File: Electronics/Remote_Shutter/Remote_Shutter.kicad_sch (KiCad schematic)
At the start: 15 parts, among them J1 OLED, J2 Joystick, J3 Micro Lipo pins, J4 AudioJack3, SW1 SW_SPDT, SW2 SW_SPDT, U1 Xiao, U2 PC817, U3 PC817

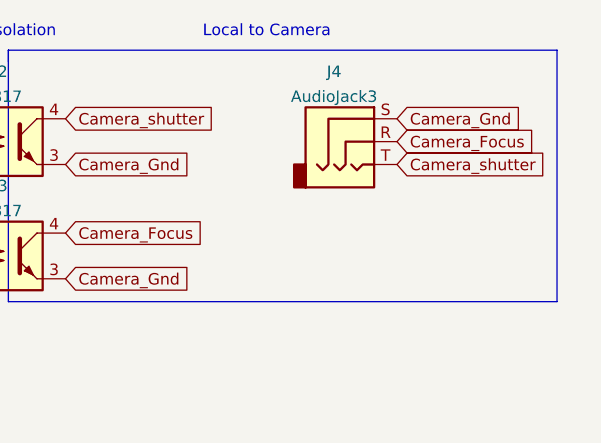
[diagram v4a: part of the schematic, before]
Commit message: fixed footprint for the TRS also made the PCB smaller and routed it.
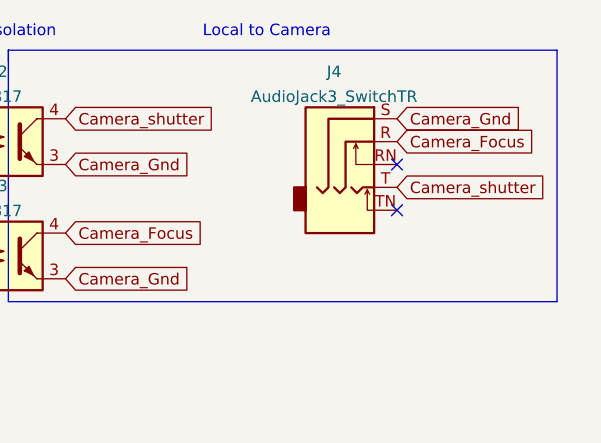
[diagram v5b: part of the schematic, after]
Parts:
- removed J4: AudioJack3, cubepattern:CUI_SJ1-3514, symbol Connector:AudioJack3
- added J4: AudioJack3_SwitchTR, cubepattern:SWITCHCRAFT_35RAPC2BH3, symbol Connector:AudioJack3_SwitchTR
- R1, R2, R3, R4: footprint Resistor_THT:R_Axial_DIN0207_L6.3mm_D2.5mm_P10.16mm_Horizontal -> Resistor_THT:R_Axial_DIN0204_L3.6mm_D1.6mm_P7.62mm_Horizontal
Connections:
- net Camera_Focus: now also J4.R
- net Camera_Gnd: now also J4.S
- net Camera_shutter: now also J4.T
- no-connect marks 4 -> 6
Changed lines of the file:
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@@
   (no_connect (at 40.64 19.05))
   (no_connect (at 43.18 19.05))
+  (no_connect (at 148.59 35.56))
+  (no_connect (at 148.59 30.48))
   (wire (pts (xy 91.44 38.1) (xy 96.52 38.1))
     (stroke (width 0) (type default) (color 0 0 0 0))
@@
     (stroke (width 0) (type default) (color 0 0 0 0))
   )
+  (wire (pts (xy 78.74 63.5) (xy 78.74 68.58))
+    (stroke (width 0) (type default) (color 0 0 0 0))
+  )
+  (wire (pts (xy 74.93 59.69) (xy 78.74 59.69))
+    (stroke (width 0) (type default) (color 0 0 0 0))
+  )
+  (polyline (pts (xy 166.37 17.78) (xy 105.41 17.78))
+    (stroke (width 0) (type default) (color 0 0 0 0))
+  )
+  (wire (pts (xy 86.36 30.48) (xy 96.52 30.48))
+    (stroke (width 0) (type default) (color 0 0 0 0))
+  )
+  (polyline (pts (xy 105.41 17.78) (xy 105.41 19.05))
+    (stroke (width 0) (type default) (color 0 0 0 0))
+  )
+  (wire (pts (xy 59.69 52.07) (xy 49.53 52.07))
+    (stroke (width 0) (type default) (color 0 0 0 0))
+  )
+  (polyline (pts (xy 15.24 71.12) (xy 15.24 60.96))
+    (stroke (width 0) (type default) (color 0 0 0 0))
+  )
   (wire (pts (xy 78.74 59.69) (xy 78.74 63.5))
-    (stroke (width 0) (type default) (color 0 0 0 0))
-  )
-  (wire (pts (xy 74.93 59.69) (xy 78.74 59.69))
-    (stroke (width 0) (type default) (color 0 0 0 0))
-  )
-  (polyline (pts (xy 166.37 17.78) (xy 105.41 17.78))
-    (stroke (width 0) (type default) (color 0 0 0 0))
-  )
-  (wire (pts (xy 86.36 30.48) (xy 96.52 30.48))
-    (stroke (width 0) (type default) (color 0 0 0 0))
-  )
-  (polyline (pts (xy 105.41 17.78) (xy 105.41 19.05))
-    (stroke (width 0) (type default) (color 0 0 0 0))
-  )
-  (wire (pts (xy 59.69 52.07) (xy 49.53 52.07))
-    (stroke (width 0) (type default) (color 0 0 0 0))
-  )
-  (polyline (pts (xy 15.24 71.12) (xy 15.24 60.96))
-    (stroke (width 0) (type default) (color 0 0 0 0))
-  )
-  (wire (pts (xy 78.74 63.5) (xy 78.74 68.58))
     (stroke (width 0) (type default) (color 0 0 0 0))
   )
@@
     )
   )
-  (global_label "Camera_shutter" (shape input) (at 148.59 30.48 0) (fields_autoplaced)
-    (effects (font (size 1.27 1.27)) (justify left))
-    (property "Intersheet References" "${INTERSHEET_REFS}" (id 0) (at 165.7593 30.4006 0)
+  (global_label "Camera_shutter" (shape input) (at 148.59 33.02 0) (fields_autoplaced)
+    (effects (font (size 1.27 1.27)) (justify left))
+    (property "Intersheet References" "${INTERSHEET_REFS}" (id 0) (at 165.7593 32.9406 0)
       (effects (font (size 1.27 1.27)) (justify left) hide)
     )
@@
   (symbol (lib_id "power:+5V") (at 24.13 49.53 90) (unit 1)
     (in_bom yes) (on_board yes) (fields_autoplaced)
-    (property "Reference" "#PWR?" (id 0) (at 27.94 49.53 0)
+    (property "Reference" "#PWR0102" (id 0) (at 27.94 49.53 0)
       (effects (font (size 1.27 1.27)) hide)
     )
@@
     )
     (pin "1")
+  )
+  (symbol (lib_id "Connector:AudioJack3_SwitchTR") (at 143.51 27.94 0) (unit 1)
+    (in_bom yes) (on_board yes) (fields_autoplaced)
+    (property "Reference" "J4" (id 0) (at 141.605 20.1635 0))
+    (property "Value" "AudioJack3_SwitchTR" (id 1) (at 141.605 22.9386 0))
+    (property "Footprint" "cubepattern:SWITCHCRAFT_35RAPC2BH3" (id 2) (at 143.51 27.94 0)
+      (effects (font (size 1.27 1.27)) hide)
+    )
+    (property "Datasheet" "~" (id 3) (at 143.51 27.94 0)
+      (effects (font (size 1.27 1.27)) hide)
+    )
+    (pin "R")
+    (pin "RN")
+    (pin "S")
+    (pin "T")
+    (pin "TN")
   )
   (symbol (lib_id "Device:R_Small") (at 88.9 38.1 90) (unit 1)
@@
     (property "Reference" "R4" (id 0) (at 88.9 33.3969 90))
     (property "Value" "220ohm" (id 1) (at 88.9 36.172 90))
-    (property "Footprint" "Resistor_THT:R_Axial_DIN0207_L6.3mm_D2.5mm_P10.16mm_Horizontal" (id 2) (at 88.9 38.1 0)
+    (property "Footprint" "Resistor_THT:R_Axial_DIN0204_L3.6mm_D1.6mm_P7.62mm_Horizontal" (id 2) (at 88.9 38.1 0)
       (effects (font (size 1.27 1.27)) hide)
     )
@@
     (property "Reference" "R3" (id 0) (at 88.9 20.6969 90))
     (property "Value" "220ohm" (id 1) (at 88.9 23.472 90))
-    (property "Footprint" "Resistor_THT:R_Axial_DIN0207_L6.3mm_D2.5mm_P10.16mm_Horizontal" (id 2) (at 88.9 25.4 0)
+    (property "Footprint" "Resistor_THT:R_Axial_DIN0204_L3.6mm_D1.6mm_P7.62mm_Horizontal" (id 2) (at 88.9 25.4 0)
       (effects (font (size 1.27 1.27)) hide)
     )
@@
   (symbol (lib_id "power:GND") (at 24.13 52.07 270) (unit 1)
     (in_bom yes) (on_board yes) (fields_autoplaced)
-    (property "Reference" "#PWR?" (id 0) (at 17.78 52.07 0)
+    (property "Reference" "#PWR0101" (id 0) (at 17.78 52.07 0)
       (effects (font (size 1.27 1.27)) hide)
     )
@@
     (property "Reference" "R1" (id 0) (at 62.23 54.9869 90))
     (property "Value" "75ohm" (id 1) (at 62.23 57.762 90))
-    (property "Footprint" "Resistor_THT:R_Axial_DIN0207_L6.3mm_D2.5mm_P10.16mm_Horizontal" (id 2) (at 62.23 59.69 0)
+    (property "Footprint" "Resistor_THT:R_Axial_DIN0204_L3.6mm_D1.6mm_P7.62mm_Horizontal" (id 2) (at 62.23 59.69 0)
       (effects (font (size 1.27 1.27)) hide)
     )
@@
     (pin "1")
     (pin "2")
-  )
-  (symbol (lib_id "Connector:AudioJack3") (at 143.51 27.94 0) (unit 1)
-    (in_bom yes) (on_board yes) (fields_autoplaced)
-    (property "Reference" "J4" (id 0) (at 141.605 20.1635 0))
-    (property "Value" "AudioJack3" (id 1) (at 141.605 22.9386 0))
-    (property "Footprint" "cubepattern:CUI_SJ1-3514" (id 2) (at 143.51 27.94 0)
-      (effects (font (size 1.27 1.27)) hide)
-    )
-    (property "Datasheet" "~" (id 3) (at 143.51 27.94 0)
-      (effects (font (size 1.27 1.27)) hide)
-    )
-    (pin "R")
-    (pin "S")
-    (pin "T")
   )
   (symbol (lib_id "power:GND") (at 88.9 60.96 90) (unit 1)
@@
     (property "Reference" "R2" (id 0) (at 62.23 63.8769 90))
     (property "Value" "10ohm" (id 1) (at 62.23 66.652 90))
-    (property "Footprint" "Resistor_THT:R_Axial_DIN0207_L6.3mm_D2.5mm_P10.16mm_Horizontal" (id 2) (at 62.23 68.58 0)
+    (property "Footprint" "Resistor_THT:R_Axial_DIN0204_L3.6mm_D1.6mm_P7.62mm_Horizontal" (id 2) (at 62.23 68.58 0)
       (effects (font (size 1.27 1.27)) hide)
     )
@@
   )
   (symbol_instances
+    (path "/b4f4fd8c-2bd4-42bb-83f4-91cfb4502a52"
+      (reference "#PWR0101") (unit 1) (value "GND") (footprint "")
+    )
+    (path "/228ec2f0-c566-4d23-b3f1-fe5d842defc4"
+      (reference "#PWR0102") (unit 1) (value "+5V") (footprint "")
+    )
     (path "/0dda9a3a-67e1-426d-8cd7-37bed7b3a5c2"
       (reference "#PWR0103") (unit 1) (value "GND") (footprint "")
@@
       (reference "#PWR0112") (unit 1) (value "GND") (footprint "")
     )
-    (path "/228ec2f0-c566-4d23-b3f1-fe5d842defc4"
-      (reference "#PWR?") (unit 1) (value "+5V") (footprint "")
-    )
-    (path "/b4f4fd8c-2bd4-42bb-83f4-91cfb4502a52"
-      (reference "#PWR?") (unit 1) (value "GND") (footprint "")
-    )
     (path "/8cb55fe4-e0f1-400c-8abb-b081e431a032"
       (reference "D1") (unit 1) (value "Red") (footprint "LED_THT:LED_D3.0mm")
@@
       (reference "J3") (unit 1) (value "Micro Lipo pins") (footprint "Connector_PinSocket_2.54mm:PinSocket_1x02_P2.54mm_Vertical")
     )
-    (path "/ca4ade4b-071e-4766-bfd1-eee3b7fe162d"
-      (reference "J4") (unit 1) (value "AudioJack3") (footprint "cubepattern:CUI_SJ1-3514")
+    (path "/25e0d0b9-b4b7-4a65-bce9-b64955e223bc"
+      (reference "J4") (unit 1) (value "AudioJack3_SwitchTR") (footprint "cubepattern:SWITCHCRAFT_35RAPC2BH3")
     )
     (path "/b8dab869-c827-4181-80d6-62cae32b4e4d"
-      (reference "R1") (unit 1) (value "75ohm") (footprint "Resistor_THT:R_Axial_DIN0207_L6.3mm_D2.5mm_P10.16mm_Horizontal")
+      (reference "R1") (unit 1) (value "75ohm") (footprint "Resistor_THT:R_Axial_DIN0204_L3.6mm_D1.6mm_P7.62mm_Horizontal")
     )
     (path "/f999f196-9de3-4cc5-a73e-ea12c61d5580"
-      (reference "R2") (unit 1) (value "10ohm") (footprint "Resistor_THT:R_Axial_DIN0207_L6.3mm_D2.5mm_P10.16mm_Horizontal")
+      (reference "R2") (unit 1) (value "10ohm") (footprint "Resistor_THT:R_Axial_DIN0204_L3.6mm_D1.6mm_P7.62mm_Horizontal")
     )
     (path "/4a583b03-7ba0-42d6-ac20-d9bd4ec5453d"
-      (reference "R3") (unit 1) (value "220ohm") (footprint "Resistor_THT:R_Axial_DIN0207_L6.3mm_D2.5mm_P10.16mm_Horizontal")
+      (reference "R3") (unit 1) (value "220ohm") (footprint "Resistor_THT:R_Axial_DIN0204_L3.6mm_D1.6mm_P7.62mm_Horizontal")
     )
     (path "/2a88d07d-3256-48f8-9a69-efbd4975a15a"
-      (reference "R4") (unit 1) (value "220ohm") (footprint "Resistor_THT:R_Axial_DIN0207_L6.3mm_D2.5mm_P10.16mm_Horizontal")
+      (reference "R4") (unit 1) (value "220ohm") (footprint "Resistor_THT:R_Axial_DIN0204_L3.6mm_D1.6mm_P7.62mm_Horizontal")
     )
     (path "/9b9bebe1-6e72-41f1-8bcc-e007286966c7"
